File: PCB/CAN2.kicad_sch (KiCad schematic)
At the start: 7 parts, among them U3 ISO1044BD

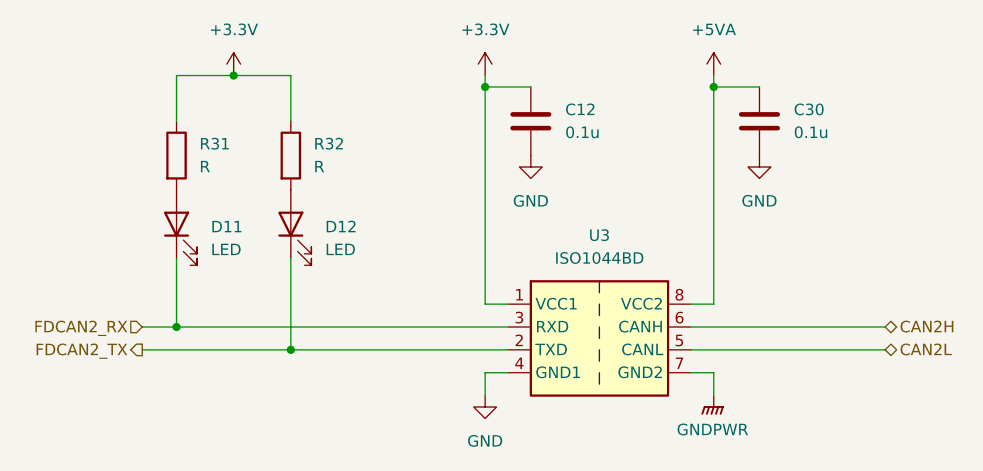
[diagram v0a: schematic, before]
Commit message: 電源以外配線おわり
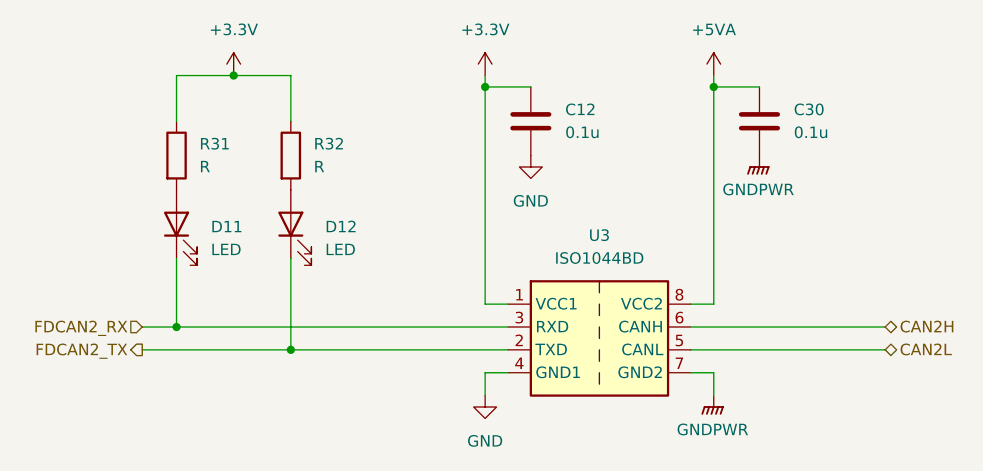
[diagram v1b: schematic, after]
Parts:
- C12, C30: footprint Capacitor_SMD:C_0402_1005Metric_Pad0.74x0.62mm_HandSolder -> Capacitor_SMD:C_0603_1608Metric_Pad1.08x0.95mm_HandSolder
- R31, R32: footprint Resistor_SMD:R_0402_1005Metric_Pad0.72x0.64mm_HandSolder -> Resistor_SMD:R_0603_1608Metric_Pad0.98x0.95mm_HandSolder
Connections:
- net GND: no longer C30.2
- net GNDPWR: now also C30.2
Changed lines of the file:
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@@
-	)
-	(symbol
-		(lib_id "power:GND")
-		(at 173.99 76.2 0)
-		(unit 1)
-		(exclude_from_sim no)
-		(in_bom yes)
-		(on_board yes)
-		(dnp no)
-		(fields_autoplaced yes)
-		(property "Reference" "#PWR055"
-			(at 173.99 82.55 0)
-			(effects
-				(font
-					(size 1.27 1.27)
-				)
-				(hide yes)
-			)
-		)
-		(property "Value" "GND"
-			(at 173.99 81.28 0)
-			(effects
-				(font
-					(size 1.27 1.27)
-				)
-			)
-		)
-		(property "Footprint" ""
-			(at 173.99 76.2 0)
-			(effects
-				(font
-					(size 1.27 1.27)
-				)
-				(hide yes)
-			)
-		)
-		(property "Datasheet" ""
-			(at 173.99 76.2 0)
-			(effects
-				(font
-					(size 1.27 1.27)
-				)
-				(hide yes)
-			)
-		)
-		(property "Description" "Power symbol creates a global label with name \"GND\" , ground"
-			(at 173.99 76.2 0)
-			(effects
-				(font
-					(size 1.27 1.27)
-				)
-				(hide yes)
-			)
-		)
-		(pin "1"
-		)
-		(instances
-			(project "kaniharu"
-				(path "/8cdd0db5-06ad-47be-921f-3bd5b446781a/356f2d0c-296b-4604-99ff-d255dfa1c102"
-					(reference "#PWR055")
-					(unit 1)
-				)
-			)
-		)
 	)
 	(symbol
@@
 			)
 		)
-		(property "Footprint" "Capacitor_SMD:C_0402_1005Metric_Pad0.74x0.62mm_HandSolder"
+		(property "Footprint" "Capacitor_SMD:C_0603_1608Metric_Pad1.08x0.95mm_HandSolder"
 			(at 149.5552 76.2 0)
 			(effects
@@
 			)
 		)
-		(property "Footprint" "Resistor_SMD:R_0402_1005Metric_Pad0.72x0.64mm_HandSolder"
+		(property "Footprint" "Resistor_SMD:R_0603_1608Metric_Pad0.98x0.95mm_HandSolder"
 			(at 107.442 76.2 90)
 			(effects
@@
 			)
 		)
-		(property "Footprint" "Resistor_SMD:R_0402_1005Metric_Pad0.72x0.64mm_HandSolder"
+		(property "Footprint" "Resistor_SMD:R_0603_1608Metric_Pad0.98x0.95mm_HandSolder"
 			(at 120.142 76.2 90)
 			(effects
@@
 			)
 		)
-		(property "Footprint" "Capacitor_SMD:C_0402_1005Metric_Pad0.74x0.62mm_HandSolder"
+		(property "Footprint" "Capacitor_SMD:C_0603_1608Metric_Pad1.08x0.95mm_HandSolder"
 			(at 174.9552 76.2 0)
 			(effects
@@
 					(unit 1)
 				)
+			)
+		)
+	)
+	(symbol
+		(lib_id "power:GNDPWR")
+		(at 173.99 76.2 0)
+		(unit 1)
+		(exclude_from_sim no)
+		(in_bom yes)
+		(on_board yes)
+		(dnp no)
+		(fields_autoplaced yes)
+		(property "Reference" "#PWR055"
+			(at 173.99 81.28 0)
+			(effects
+				(font
+					(size 1.27 1.27)
+				)
+				(hide yes)
+			)
+		)
+		(property "Value" "GNDPWR"
+			(at 173.863 80.01 0)
+			(effects
+				(font
+					(size 1.27 1.27)
+				)
+			)
+		)
+		(property "Footprint" ""
+			(at 173.99 77.47 0)
+			(effects
+				(font
+					(size 1.27 1.27)
+				)
+				(hide yes)
+			)
+		)
+		(property "Datasheet" ""
+			(at 173.99 77.47 0)
+			(effects
+				(font
+					(size 1.27 1.27)
+				)
+				(hide yes)
+			)
+		)
+		(property "Description" "Power symbol creates a global label with name \"GNDPWR\" , global ground"
+			(at 173.99 76.2 0)
+			(effects
+				(font
+					(size 1.27 1.27)
+				)
+				(hide yes)
+			)
+		)
+		(pin "1"
+		)
+		(instances
+			(project "kaniharu"
+				(path "/8cdd0db5-06ad-47be-921f-3bd5b446781a/356f2d0c-296b-4604-99ff-d255dfa1c102"
+					(reference "#PWR055")
+					(unit 1)
+				)

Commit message: update:基板発注した
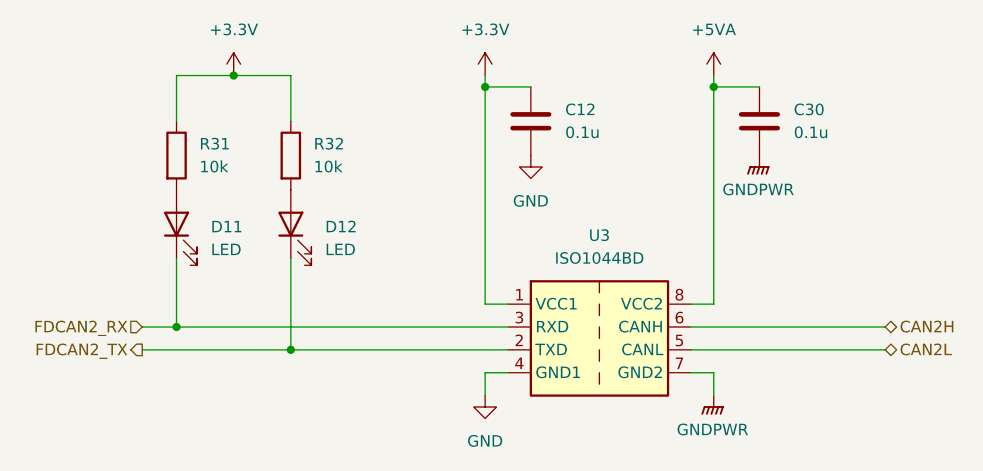
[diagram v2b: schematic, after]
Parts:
- R31, R32: value R -> 10k
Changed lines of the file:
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@@
 			)
 		)
-		(property "Value" "R"
+		(property "Value" "10k"
 			(at 111.76 77.4699 0)
 			(effects
@@
 			)
 		)
-		(property "Value" "R"
+		(property "Value" "10k"
 			(at 124.46 77.4699 0)
 			(effects
